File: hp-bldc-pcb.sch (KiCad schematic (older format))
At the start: 46 parts, among them IC101 MCP1790-5002E/DB, T102 SBC817-40LT1G, T103 SBC817-40LT1G

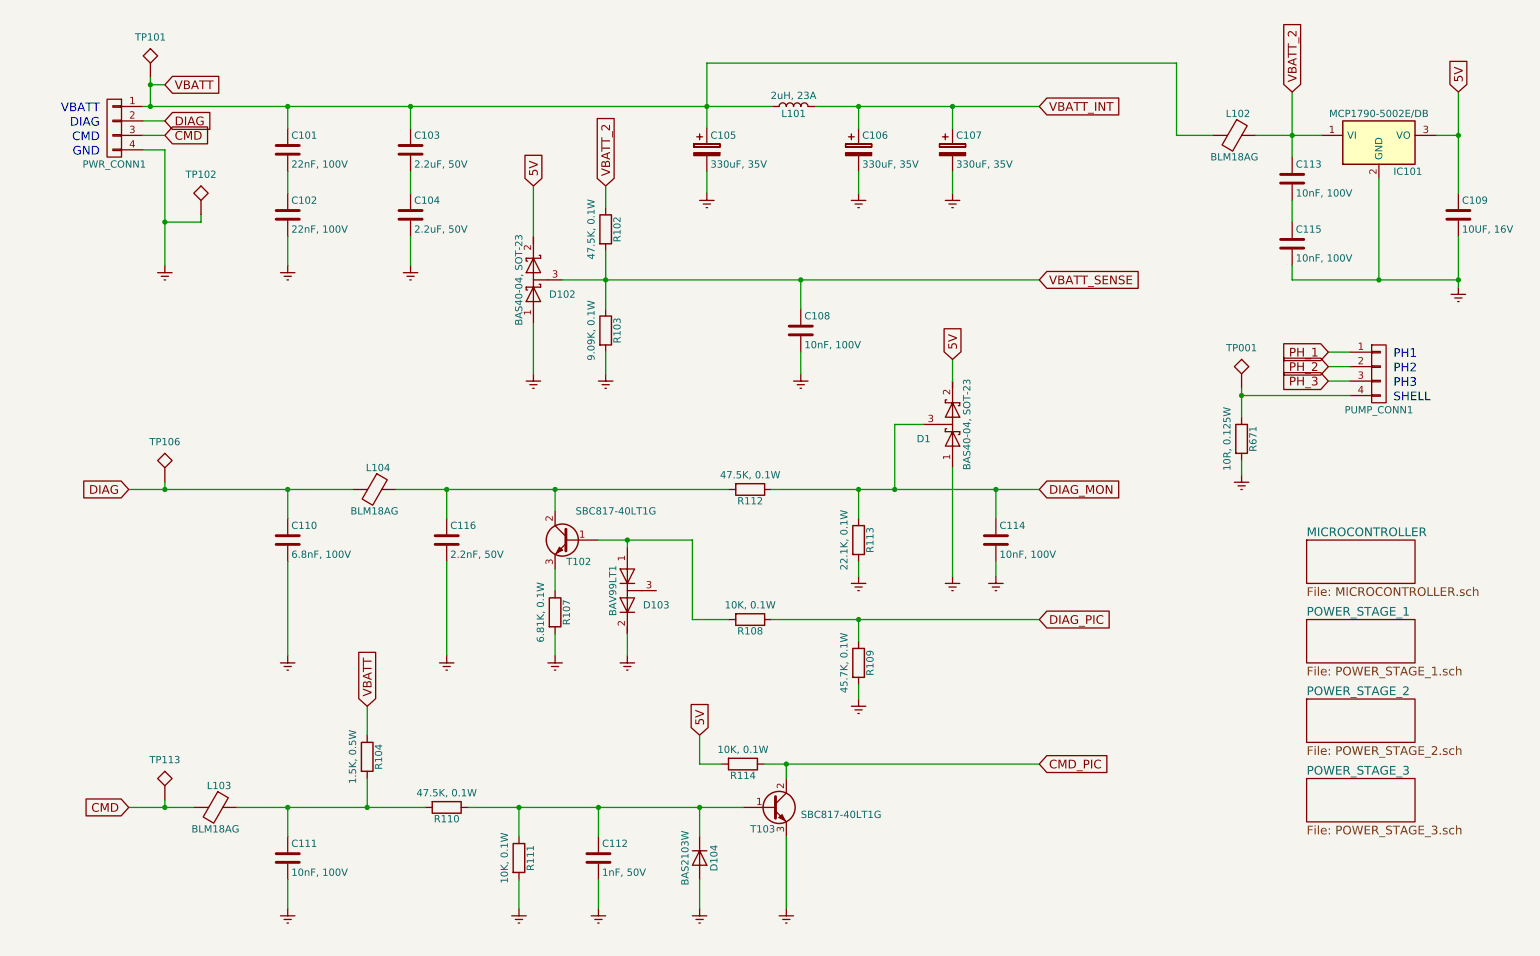
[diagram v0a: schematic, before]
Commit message: - Finished traces.  Now copper areas.
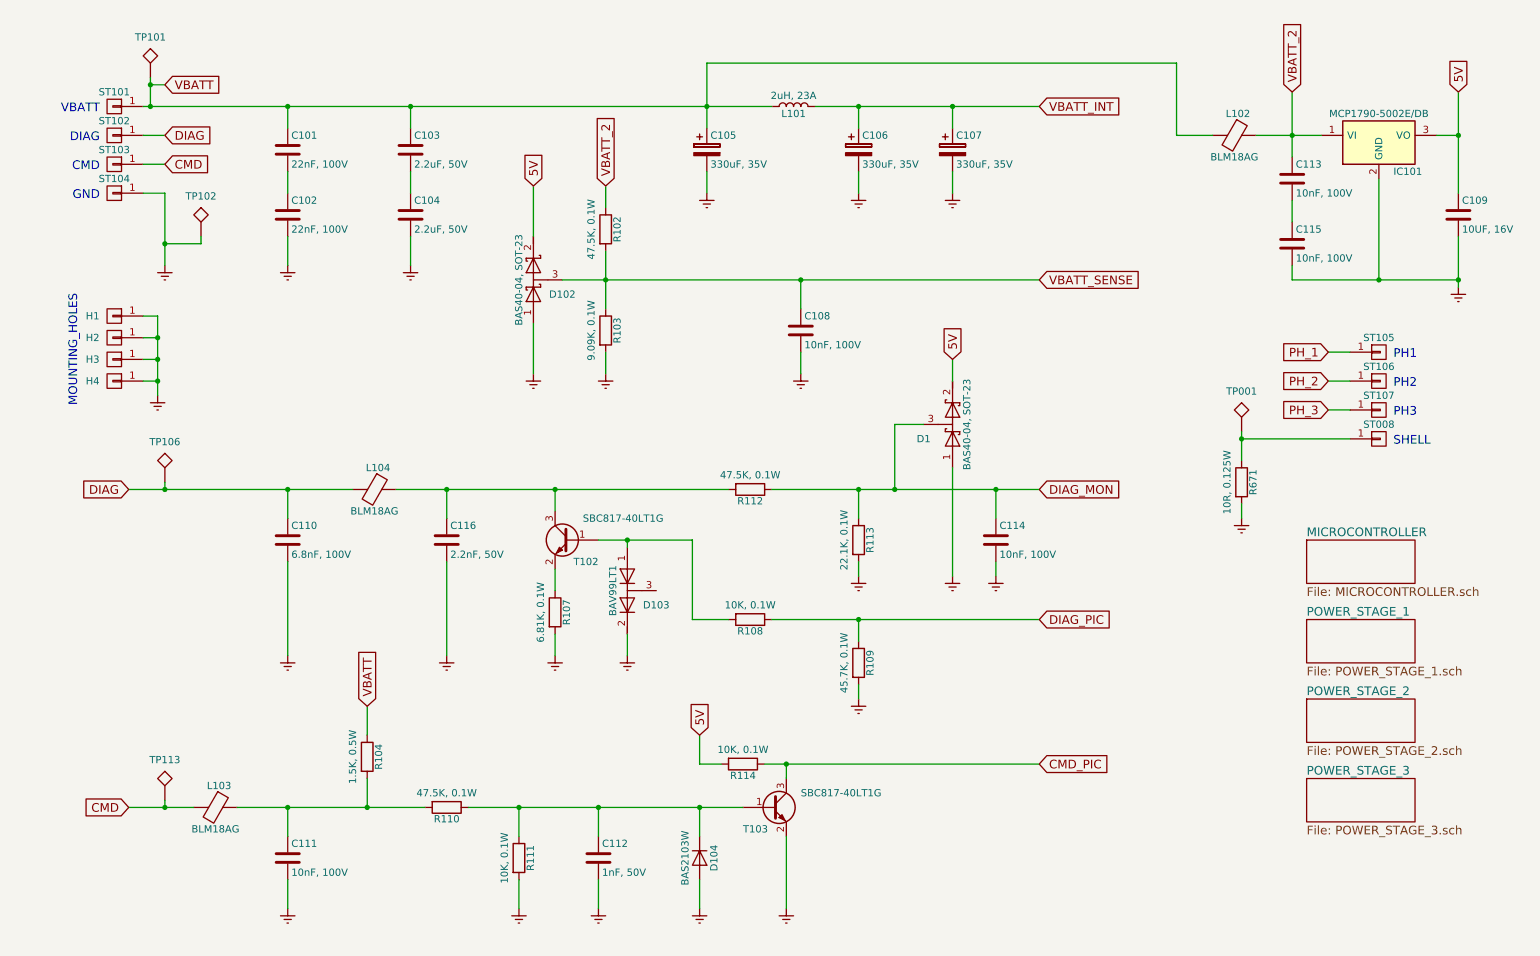
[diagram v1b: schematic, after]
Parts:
- removed PUMP_CONN1, PWR_CONN1: CONN_01X04, symbol CONN_01X04
- removed T102, T103: SBC817-40LT1G, TO_SOT_Packages_SMD:SOT-23, symbol Q_NPN_BCE
- added H1, H2, H3, H4: CONN_01X01, hp-bldc-pcb:MOUNTING_HOLE_FOR_4-40, symbol CONN_01X01
- added ST008, ST101, ST102, ST103, ST104, ST105, ST106, ST107: CONN_01X01, hp-bldc-pcb:WIRE_HARNESS_THRU_HOLE, symbol CONN_01X01
- added T102, T103: SBC817-40LT1G, TO_SOT_Packages_SMD:SOT-23, symbol Q_NPN_BEC
- C108: footprint Capacitors_SMD:C_1206 -> Capacitors_SMD:C_0603
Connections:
- net CMD: now also ST103.1 (P1)
- net CMD_PIC: now also T103.3 (C)
- net DIAG: now also ST102.1 (P1)
- net Earth: now also H1.1 (P1), H2.1 (P1), H3.1 (P1), H4.1 (P1), ST104.1 (P1), T103.2 (E)
- net PH_1: now also ST105.1 (P1)
- net PH_2: now also ST106.1 (P1)
- net PH_3: now also ST107.1 (P1)
- net VBATT: now also ST101.1 (P1)
- net at R671.1, TP001.1: now also ST008.1 (P1)
- net at C116.1, L104.1, R112.2: now also T102.3 (C)
- net at D103.1 (A), R108.2: now also T102.1 (B)
- net at R107.1: now also T102.2 (E)
- net at C112.1, D104.1 (K), R110.1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: now also T103.1 (B)
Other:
- note added: "MOUNTING_HOLES"
- moved on the sheet: R671, TP001, TP102

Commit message: - Finished adaptation to JMS board footprint. - Added testpoints. - Changed header connector to 0.1" pitch, and tall.
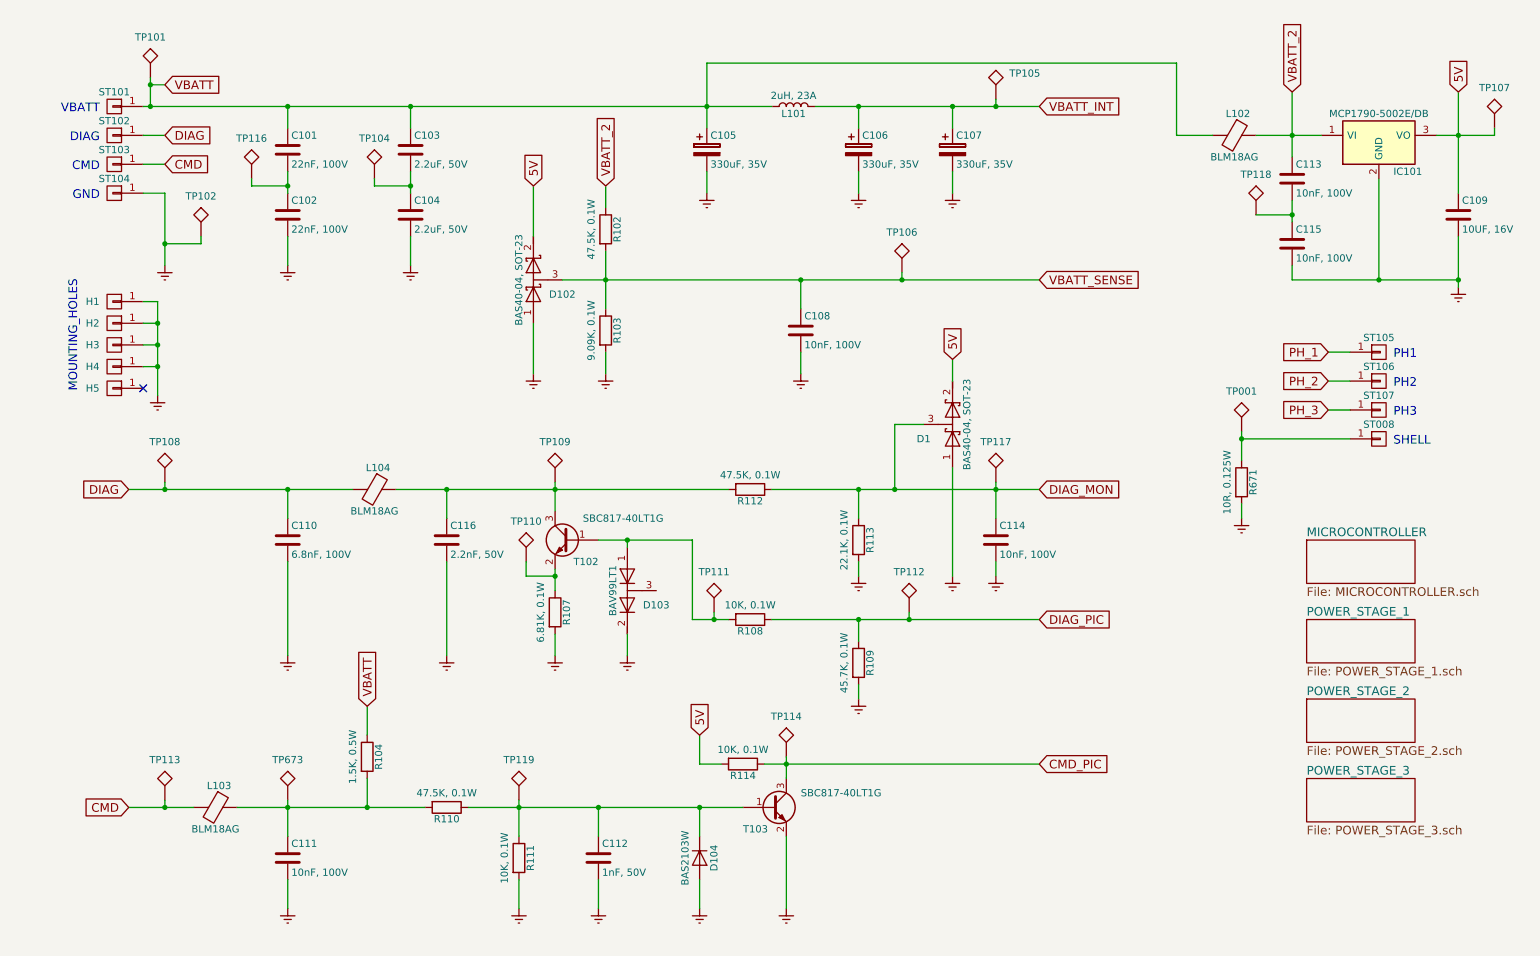
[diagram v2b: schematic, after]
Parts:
- added H5: CONN_01X01, hp-bldc-pcb:ENCLOSURE_MOUNTING_HOLE, symbol CONN_01X01
- added TP104, TP105, TP106, TP107, TP109, TP110, TP111, TP112, TP114, TP116, TP117, TP118, TP119, TP673: TEST, hp-bldc-pcb:TEST_POINT_40mil, symbol TEST
- H1, H2, H3, H4: footprint hp-bldc-pcb:MOUNTING_HOLE_FOR_4-40 -> hp-bldc-pcb:ENCLOSURE_MOUNTING_HOLE
- ST008, ST101, ST102, ST103, ST104, ST105, ST106, ST107: footprint hp-bldc-pcb:WIRE_HARNESS_THRU_HOLE -> hp-bldc-pcb:BIG_RECT_PAD
- TP001, TP101, TP102, TP113: footprint Measurement_Points:Measurement_Point_Round-SMD-Pad_Big -> hp-bldc-pcb:TEST_POINT_40mil
- TP108: renamed from TP106; footprint Measurement_Points:Measurement_Point_Round-SMD-Pad_Big -> hp-bldc-pcb:TEST_POINT_40mil
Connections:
- net 5V: now also TP107.1
- net CMD_PIC: now also TP114.1
- net DIAG_MON: now also TP117.1
- net DIAG_PIC: now also TP112.1
- net VBATT_INT: now also TP105.1
- net VBATT_SENSE: now also TP106.1
- net at C101.2, C102.1: now also TP116.1
- net at C103.2, C104.1: now also TP104.1
- net at C113.2, C115.1: now also TP118.1
- net at C116.1, L104.1, R112.2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: now also TP109.1
- net at R107.1, T102.2 (E): now also TP110.1
- net at D103.1 (A), R108.2, T102.1 (B): now also TP111.1
- net at C111.1, L103.1, R104.2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: now also TP673.1
- net at C112.1, D104.1 (K), R110.1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: now also TP119.1
- no-connect marks 0 -> 1
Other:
- moved on the sheet: H1, H2, H3, H4

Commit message: - Minor changes to silkscreen. - Minor changes to BOM. - Additions to Readme file. - Page layout changed in schematic.
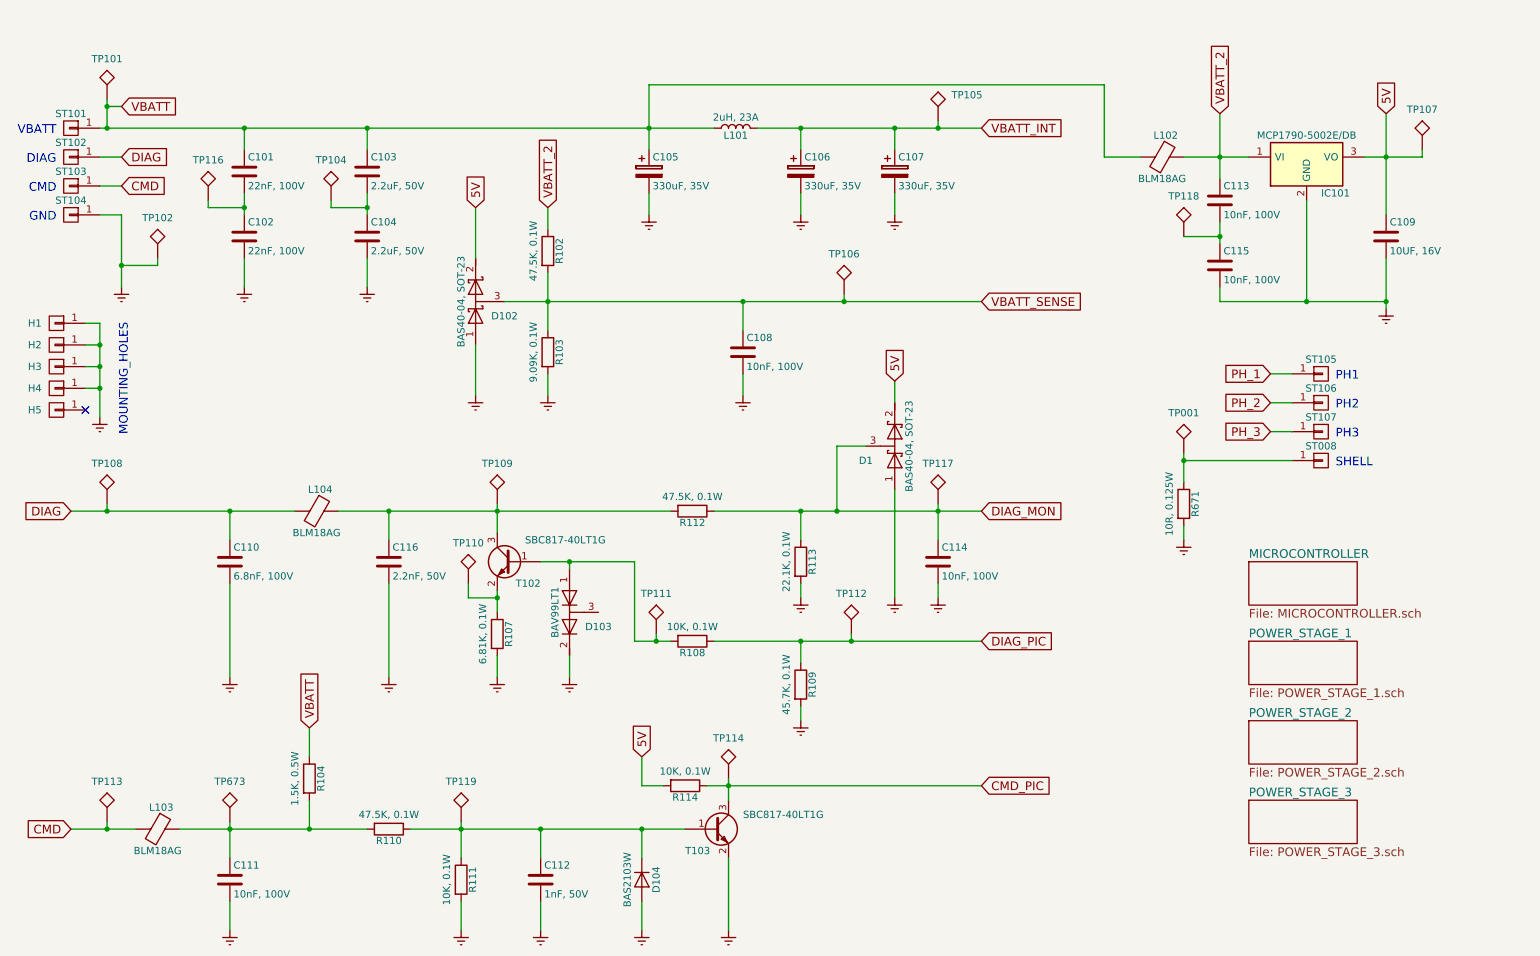
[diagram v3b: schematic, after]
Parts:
- IC101: footprint TO_SOT_Packages_SMD:SOT-223 -> hp-bldc-pcb:SOT-223
- L101: footprint Inductors_SMD:L_Wuerth_HCI-1365 -> hp-bldc-pcb:L_Wuerth_HCI-1365
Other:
- moved on the sheet: C101, C102, C103, C104, C105, C106, C107, C108, C109, C110, C111, C112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

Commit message: - Added TP411 at JMS request.  This was needed to test the NTC during ICT.
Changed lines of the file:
@@
 $EndComp
 Wire Wire Line
-	2100 1750 2100 1850
-Wire Wire Line
-	2100 1850 2100 1900
-Wire Wire Line
-	1100 1300 1150 1300
-Wire Wire Line
-	1150 1300 2100 1300
-Wire Wire Line
-	2100 1300 2950 1300
-Wire Wire Line
-	2950 1300 4900 1300
-Wire Wire Line
-	4900 1300 5350 1300
+	2100 1750 2100 1900
+Wire Wire Line
+	1100 1300 5350 1300
 Wire Wire Line
 	2100 1300 2100 1450
@@
 Connection ~ 2100 1300
 Wire Wire Line
-	2950 1750 2950 1850
-Wire Wire Line
-	2950 1850 2950 1900
+	2950 1750 2950 1900
 Wire Wire Line
 	2950 2200 2950 2400
 Wire Wire Line
-	4900 1000 4900 1300
-Wire Wire Line
-	4900 1300 4900 1450
+	4900 1000 4900 1450
 Connection ~ 2950 1300
 Connection ~ 4900 1300
@@
 	4900 1750 4900 1900
 Wire Wire Line
-	5650 1300 5950 1300
-Wire Wire Line
-	5950 1300 6600 1300
-Wire Wire Line
-	6600 1300 6900 1300
-Wire Wire Line
-	6900 1300 7200 1300
+	5650 1300 7200 1300
 Wire Wire Line
 	6600 1300 6600 1450
@@
 	4200 3000 4200 3150
 Wire Wire Line
-	4200 2300 4200 2500
-Wire Wire Line
-	4200 2500 4200 2700
-Wire Wire Line
-	3900 2500 4200 2500
-Wire Wire Line
-	4200 2500 5550 2500
-Wire Wire Line
-	5550 2500 6250 2500
-Wire Wire Line
-	6250 2500 7200 2500
+	4200 2300 4200 2700
+Wire Wire Line
+	3900 2500 7200 2500
 Connection ~ 4200 2500
 Wire Wire Line
@@
 	8300 1500 8050 1500
 Wire Wire Line
-	8600 1500 8850 1500
-Wire Wire Line
-	8850 1500 9050 1500
+	8600 1500 9050 1500
 Connection ~ 8850 1500
 Wire Wire Line
-	8850 1950 8850 2050
-Wire Wire Line
-	8850 2050 8850 2100
-Wire Wire Line
-	10000 2200 10000 2500
-Wire Wire Line
-	10000 2500 10000 2550
+	8850 1950 8850 2100
+Wire Wire Line
+	10000 2200 10000 2550
 Wire Wire Line
 	8850 2400 8850 2500
 Wire Wire Line
-	8850 2500 9450 2500
-Wire Wire Line
-	9450 2500 10000 2500
+	8850 2500 10000 2500
 Connection ~ 10000 2500
 Wire Wire Line
-	10000 1200 10000 1500
-Wire Wire Line
-	10000 1500 10000 1900
-Wire Wire Line
-	9850 1500 10000 1500
-Wire Wire Line
-	10000 1500 10250 1500
+	10000 1200 10000 1900
+Wire Wire Line
+	9850 1500 10250 1500
 Connection ~ 10000 1500
 Wire Wire Line
@@
 	8050 1000 8050 1500
 Wire Wire Line
-	8850 1200 8850 1500
-Wire Wire Line
-	8850 1500 8850 1650
-Wire Wire Line
-	900  3950 1150 3950
-Wire Wire Line
-	1150 3950 2000 3950
-Wire Wire Line
-	2000 3950 2450 3950
+	8850 1200 8850 1650
+Wire Wire Line
+	900  3950 2450 3950
 Wire Wire Line
 	2000 4150 2000 3950
 Connection ~ 2000 3950
 Wire Wire Line
-	2750 3950 3100 3950
-Wire Wire Line
-	3100 3950 3850 3950
-Wire Wire Line
-	3850 3950 5050 3950
+	2750 3950 5050 3950
 Wire Wire Line
 	3100 3950 3100 4150
 Wire Wire Line
-	3850 3900 3850 3950
-Wire Wire Line
-	3850 3950 3850 4100
+	3850 3900 3850 4100
 Connection ~ 3100 3950
 Wire Wire Line
-	3850 4500 3850 4550
-Wire Wire Line
-	3850 4550 3850 4650
-Wire Wire Line
-	4150 4300 4350 4300
-Wire Wire Line
-	4350 4300 4800 4300
+	3850 4500 3850 4650
+Wire Wire Line
+	4150 4300 4800 4300
 Wire Wire Line
 	4350 4300 4350 4350
 Connection ~ 3850 3950
 Wire Wire Line
-	5350 3950 5950 3950
-Wire Wire Line
-	5950 3950 6200 3950
-Wire Wire Line
-	6200 3950 6900 3950
-Wire Wire Line
-	6900 3950 7200 3950
+	5350 3950 7200 3950
 Wire Wire Line
 	5950 3950 5950 4150
 Connection ~ 5950 3950
 Wire Wire Line
-	6900 3900 6900 3950
-Wire Wire Line
-	6900 3950 6900 4150
+	6900 3900 6900 4150
 Connection ~ 6900 3950
 Wire Wire Line
@@
 	6900 4450 6900 4550
 Wire Wire Line
-	5350 4850 5950 4850
-Wire Wire Line
-	5950 4850 6300 4850
-Wire Wire Line
-	6300 4850 7200 4850
+	5350 4850 7200 4850
 Wire Wire Line
 	4800 4300 4800 4850
 Wire Wire Line
-	4800 4850 4950 4850
-Wire Wire Line
-	4950 4850 5050 4850
+	4800 4850 5050 4850
 Connection ~ 4350 4300
 Wire Wire Line
@@
 	5950 5300 5950 5400
 Wire Wire Line
-	900  6150 1150 6150
-Wire Wire Line
-	1150 6150 1350 6150
+	900  6150 1350 6150
 Wire Wire Line
 	1250 1150 1150 1150
 Wire Wire Line
-	1150 1100 1150 1150
-Wire Wire Line
-	1150 1150 1150 1300
+	1150 1100 1150 1300
 Connection ~ 1150 1300
 Wire Wire Line
 	2550 5450 2550 5650
 Wire Wire Line
-	1650 6150 2000 6150
-Wire Wire Line
-	2000 6150 2550 6150
-Wire Wire Line
-	2550 6150 2950 6150
+	1650 6150 2950 6150
 Wire Wire Line
 	2550 5950 2550 6150
 Connection ~ 2550 6150
 Wire Wire Line
-	2000 6100 2000 6150
-Wire Wire Line
-	2000 6150 2000 6350
+	2000 6100 2000 6350
 Connection ~ 2000 6150
 Wire Wire Line
-	3250 6150 3600 6150
-Wire Wire Line
-	3600 6150 4150 6150
-Wire Wire Line
-	4150 6150 4850 6150
-Wire Wire Line
-	4850 6150 5150 6150
-Wire Wire Line
-	3600 6100 3600 6150
-Wire Wire Line
-	3600 6150 3600 6350
+	3250 6150 5150 6150
+Wire Wire Line
+	3600 6100 3600 6350
 Connection ~ 3600 6150
 Wire Wire Line
@@
 Connection ~ 4850 6150
 Wire Wire Line
-	5300 5850 5450 5850
-Wire Wire Line
-	5450 5850 7200 5850
-Wire Wire Line
-	5450 5800 5450 5850
-Wire Wire Line
-	5450 5850 5450 5950
+	5300 5850 7200 5850
+Wire Wire Line
+	5450 5800 5450 5950
 Wire Wire Line
 	4850 5650 4850 5850
@@
 	9200 3000 9350 3000
 Wire Wire Line
-	8600 3550 8600 3600
-Wire Wire Line
-	8600 3600 8600 3750
+	8600 3550 8600 3750
 Wire Wire Line
 	8600 4050 8600 4150
@@
 	1100 1900 1250 1900
 Wire Wire Line
-	1250 1900 1250 2250
-Wire Wire Line
-	1250 2250 1250 2400
+	1250 1900 1250 2400
 Wire Wire Line
 	1500 2200 1500 2250
@@
 	1000 2650 1100 2650
 Wire Wire Line
-	1100 2650 1100 2800
-Wire Wire Line
-	1100 2800 1100 2950
-Wire Wire Line
-	1100 2950 1100 3100
-Wire Wire Line
-	1100 3100 1100 3300
+	1100 2650 1100 3300
 Wire Wire Line
 	1000 2800 1100 2800
